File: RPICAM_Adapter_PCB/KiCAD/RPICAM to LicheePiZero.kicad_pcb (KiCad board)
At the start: 2 copper layers, 6 parts, among them J1 RPI Camera Pin Out, U8 Lichee Pi Zero Headers

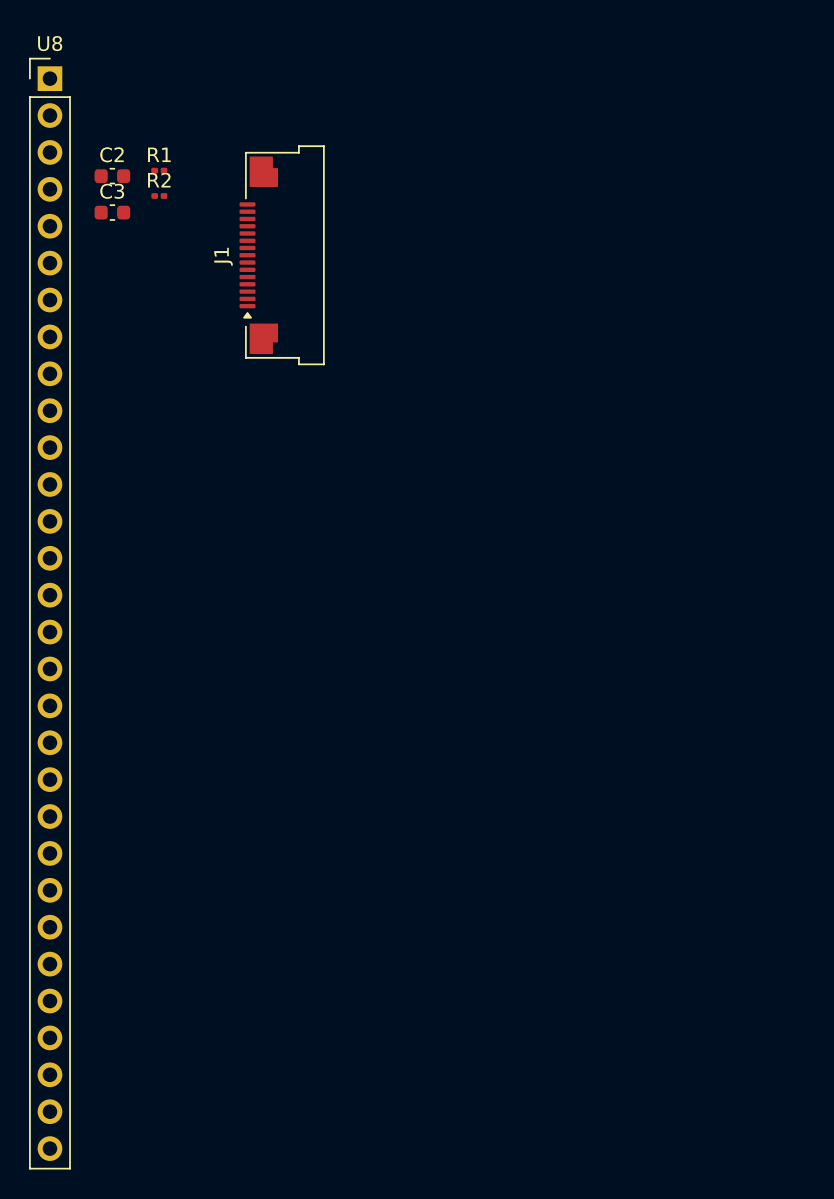
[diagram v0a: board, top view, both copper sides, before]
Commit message: This is the ordered version of the MIPI-CSI2 adapter PCB
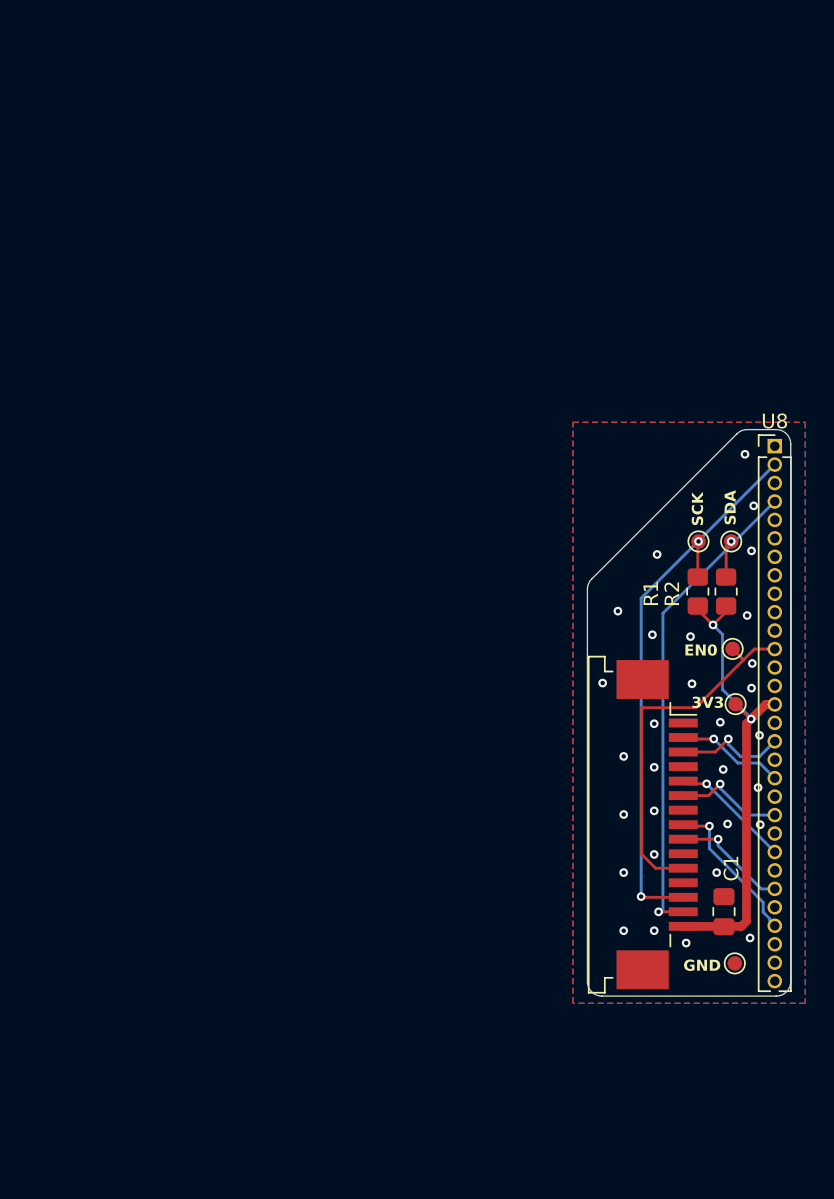
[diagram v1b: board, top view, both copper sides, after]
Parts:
- removed C2: 0.1 uF, Capacitor_SMD:C_0603_1608Metric
- removed C3: 1 uF, Capacitor_SMD:C_0603_1608Metric
- added C1: 1 uF, Capacitor_SMD:C_0805_2012Metric_Pad1.18x1.45mm_HandSolder, F.Cu at (127.4, 94.7)
- added TP1: TestPoint, TestPoint:TestPoint_Pad_D1.0mm, F.Cu at (128.2, 80.4)
- added TP2: TestPoint, TestPoint:TestPoint_Pad_D1.0mm, F.Cu at (128.2, 98.2)
- added TP3: TestPoint, TestPoint:TestPoint_Pad_D1.0mm, F.Cu at (128.0, 76.6)
- added TP4: TestPoint, TestPoint:TestPoint_Pad_D1.0mm, F.Cu at (125.7, 69.2)
- added TP5: TestPoint, TestPoint:TestPoint_Pad_D1.0mm, F.Cu at (127.9, 69.2)
- J1: value RPI Camera Pin Out -> 1-84952-5; footprint Connector_FFC-FPC:Amphenol_F32Q-1A7x1-11015_1x15-1MP_P0.5mm_Horizontal -> Connector_FFC-FPC:TE_1-84952-5_1x15-1MP_P1.0mm_Horizontal
- R1, R2: value 1K -> 4.7k; footprint Resistor_SMD:R_0201_0603Metric -> Resistor_SMD:R_0805_2012Metric_Pad1.20x1.40mm_HandSolder
- U8: footprint Connector_PinHeader_2.54mm:PinHeader_1x30_P2.54mm_Vertical -> Connector_PinHeader_1.27mm:PinHeader_1x30_P1.27mm_Vertical
- moved U8 55.9 mm to (130.9, 62.6)
- moved R2 47.6 mm to (127.5, 72.7), turned to 90 degrees
- moved R1 47.1 mm to (125.6, 72.7), turned to 90 degrees
- moved J1 46.7 mm to (122.8, 88.7), turned to -90 degrees
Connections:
- net Net-(J1-CSI_CLKN) renamed MCSI_CK_N
- net Net-(J1-CSI_CLKP) renamed MCSI_CK_P
- net Net-(J1-CSI_D0N) renamed MCSI_D0_N
- net Net-(J1-CSI_D0P) renamed MCSI_D0_P
- net Net-(J1-CSI_D1N) renamed MCSI_D1_N
- net Net-(J1-CSI_D1P) renamed MCSI_D1_P
- J1 pad 1: +3.3V -> GND
- J1 pad 10: +3.3V -> GND
- J1 pad 11: Net-(J1-CAM_EN0) -> CAM_EN0
- J1 pad 12: Net-(J1-CAM_EN1) -> unconnected-(J1-CAM_EN1-Pad12)
- J1 pad 13: Net-(J1-CAM_SCL) -> CSI_SCK
- J1 pad 14: Net-(J1-CAM_SDA) -> CSI_SDA
- J1 pad 15: +3.3V -> +3V3
- J1 pad 4: +3.3V -> GND
- J1 pad 7: +3.3V -> GND
- R1 pad 1: Net-(U8-MCSI_PWDN/PB3) -> +3V3
- R1 pad 2: Net-(J1-CAM_EN1) -> CSI_SCK
- R2 pad 1: Net-(U8-MCSI_RST/PB2) -> +3V3
- R2 pad 2: Net-(J1-CAM_EN0) -> CSI_SDA
- U8 pad 1: (no net) -> /LCD_DE
- U8 pad 10: (no net) -> /PWM0_PB4
- U8 pad 11: (no net) -> +1V2
- U8 pad 12: (no net) -> CAM_EN0
- U8 pad 13: (no net) -> +1V8
- U8 pad 14: (no net) -> /TWI0_SCK
- U8 pad 15: Net-(J1-CAM_SDA) -> +3V3
- U8 pad 16: (no net) -> /TWI0_SDA
- U8 pad 18: Net-(J1-CAM_SCL) -> /TWI1_SCK0
- U8 pad 2: (no net) -> CSI_SCK
- U8 pad 20: Net-(J1-CAM_SDA) -> /TWI1_SDA0
- U8 pad 22: (no net) -> /SPI_SCK
- U8 pad 24: (no net) -> /SPI_MOSI
- U8 pad 26: (no net) -> /SPI_MISO
- U8 pad 28: (no net) -> /SPI_CS
- U8 pad 29: +3.3V -> GND
- U8 pad 3: (no net) -> /LCD_CLK
- U8 pad 30: (no net) -> +5V
- U8 pad 4: (no net) -> CSI_SDA
- U8 pad 5: (no net) -> /MCSI_MCLK
- U8 pad 6: (no net) -> /UART2_TX
- U8 pad 7: Net-(U8-MCSI_RST/PB2) -> /UART2_RTSPB2
- U8 pad 8: (no net) -> /UART2_RX
- U8 pad 9: Net-(U8-MCSI_PWDN/PB3) -> /UART2_CTSPB3
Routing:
- net CSI_SCK: track 0.00 -> 38.9 mm, vias 0 -> 2
- net CSI_SDA: track 0.00 -> 36.0 mm, vias 0 -> 2
- net +3V3: track 0.00 -> 32.8 mm, vias 0 -> 2
- net CAM_EN0: track 0.00 -> 25.2 mm
- net MCSI_CK_N: track 0.00 -> 10.6 mm, vias 0 -> 1
- net MCSI_D1_N: track 0.00 -> 8.32 mm, vias 0 -> 1
- net MCSI_CK_P: track 0.00 -> 7.98 mm, vias 0 -> 1
- net MCSI_D0_P: track 0.00 -> 7.82 mm, vias 0 -> 1
- net MCSI_D1_P: track 0.00 -> 7.68 mm, vias 0 -> 1
- net MCSI_D0_N: track 0.00 -> 7.60 mm, vias 0 -> 1
- net GND: vias 0 -> 30
- added copper zone on B.Cu, net GND
- added copper zone on F.Cu, net GND
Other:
- board outline added: 14 x 39 mm
- board text added: "3V3"
- board text added: "EN0"
- board text added: "GND"
- board text added: "Lichee Pi Zero to MIPI-CSI2 adapter board, V1.0, Oct-2/2025"
- board text added: "SCK"
- board text added: "SDA"
